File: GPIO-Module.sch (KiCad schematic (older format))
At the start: 41 parts

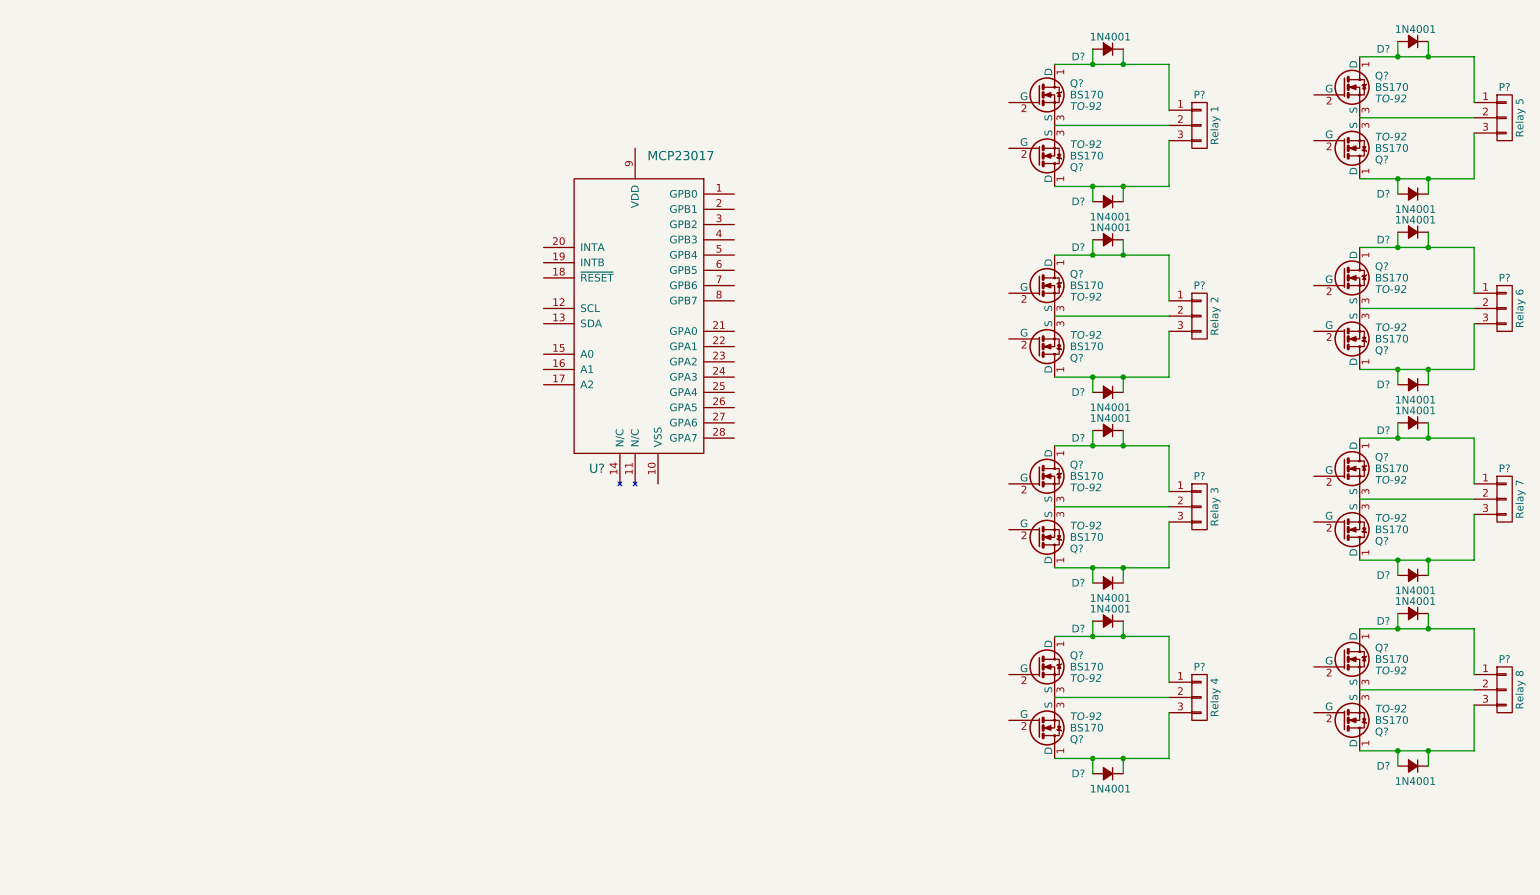
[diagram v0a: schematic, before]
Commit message: finished schematic and started pcb layout
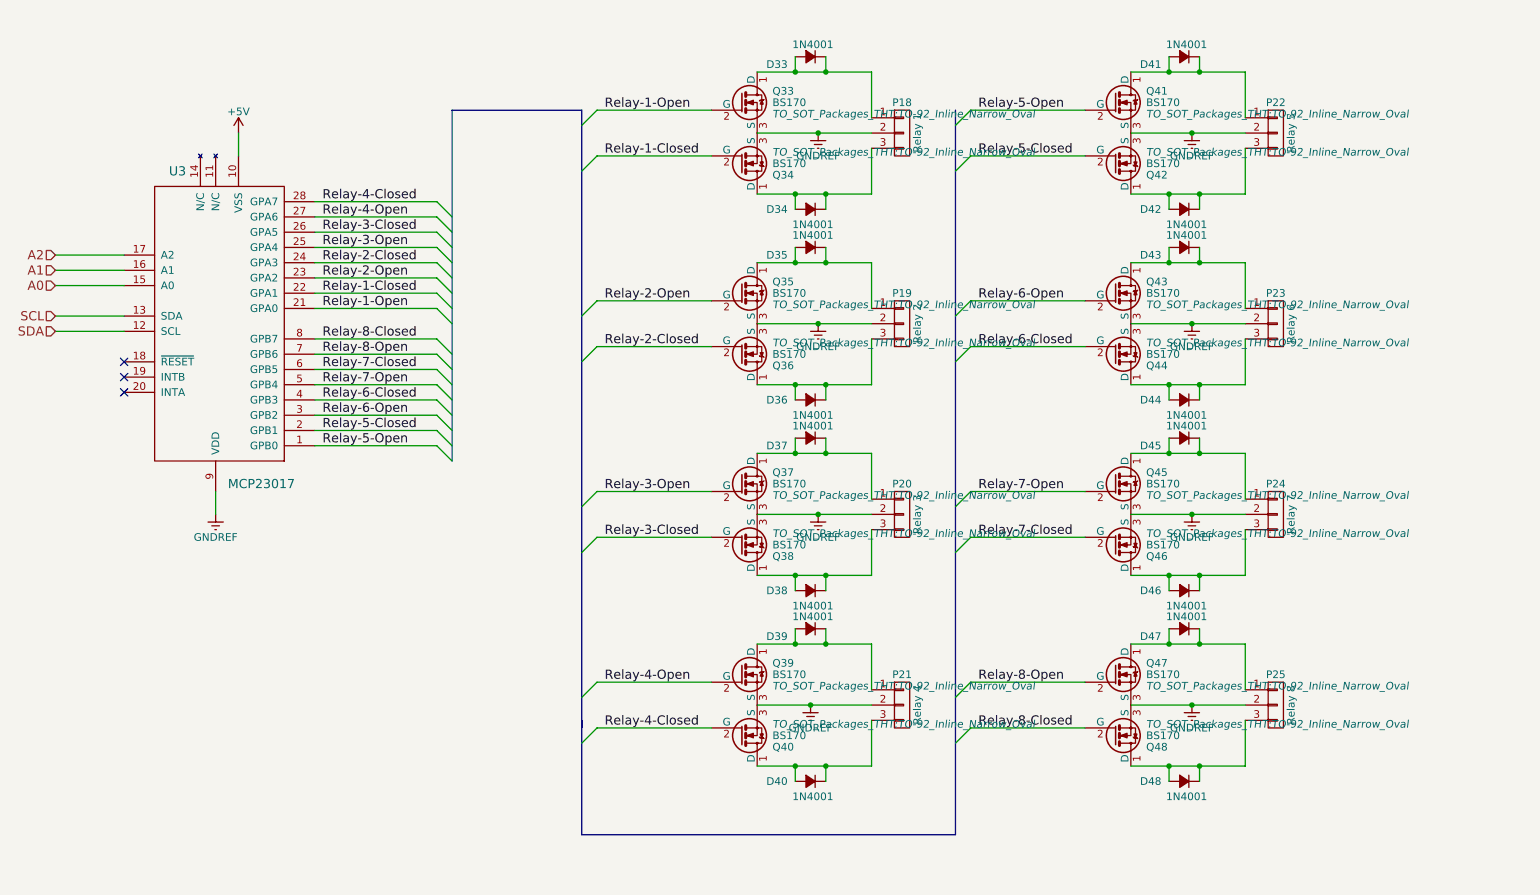
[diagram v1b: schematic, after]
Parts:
- D1, D10, D11, D12, D13, D14, D15, D16, D2, D3, D4, D5, D6, D7, D8, D9: renamed from D?; footprint (none) -> Diodes_ThroughHole:Diode_DO-41_SOD81_Horizontal_RM10
- P2, P3, P4, P5, P6, P7, P8, P9: renamed from P?; footprint (none) -> Terminal_Blocks:TerminalBlock_Pheonix_MPT-2.54mm_3pol
- Q1, Q10, Q11, Q12, Q13, Q14, Q15, Q16, Q2, Q3, Q4, Q5, Q6, Q7, Q8, Q9: renamed from Q?; footprint TO-92 -> TO_SOT_Packages_THT:TO-92_Inline_Narrow_Oval
- U1: renamed from U?; footprint (none) -> Housings_DIP:DIP-28_W7.62mm_LongPads
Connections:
- net Relay-5-Open: now reaches U1.1 (GPB0)
- net Relay-5-Open: now also Q9.2 (G)
- net +5V: now reaches U1.10 (VSS)
- net SDA: now reaches U1.12 (SCL)
- net SCL: now reaches U1.13 (SDA)
- net A0: now reaches U1.15 (A0)
- net A1: now reaches U1.16 (A1)
- net A2: now reaches U1.17 (A2)
- net Relay-5-Closed: now reaches U1.2 (GPB1)
- net Relay-5-Closed: now also Q10.2 (G)
- net Relay-1-Open: now reaches U1.21 (GPA0)
- net Relay-1-Open: now also Q1.2 (G)
- net Relay-1-Closed: now reaches U1.22 (GPA1)
- net Relay-1-Closed: now also Q2.2 (G)
- net Relay-2-Open: now reaches U1.23 (GPA2)
- net Relay-2-Open: now also Q3.2 (G)
- net Relay-2-Closed: now reaches U1.24 (GPA3)
- net Relay-2-Closed: now also Q4.2 (G)
- net Relay-3-Open: now reaches U1.25 (GPA4)
- net Relay-3-Open: now also Q5.2 (G)
- net Relay-3-Closed: now reaches U1.26 (GPA5)
- net Relay-3-Closed: now also Q6.2 (G)
- net Relay-4-Open: now reaches U1.27 (GPA6)
- net Relay-4-Open: now also Q7.2 (G)
- net Relay-4-Closed: now reaches U1.28 (GPA7)
- net Relay-4-Closed: now also Q8.2 (G)
- net Relay-6-Open: now reaches U1.3 (GPB2)
- net Relay-6-Open: now also Q11.2 (G)
- net Relay-6-Closed: now reaches U1.4 (GPB3)
- net Relay-6-Closed: now also Q12.2 (G)
- net Relay-7-Open: now reaches U1.5 (GPB4)
- net Relay-7-Open: now also Q13.2 (G)
- net Relay-7-Closed: now reaches U1.6 (GPB5)
- net Relay-7-Closed: now also Q14.2 (G)
- net Relay-8-Open: now reaches U1.7 (GPB6)
- net Relay-8-Open: now also Q15.2 (G)
- net Relay-8-Closed: now reaches U1.8 (GPB7)
- net Relay-8-Closed: now also Q16.2 (G)
- net GNDREF: now reaches U1.9 (VDD)
- net GNDREF: now also P2.2 (P2), P3.2 (P2), P4.2 (P2), P5.2 (P2), P6.2 (P2), P7.2 (P2), P8.2 (P2), P9.2 (P2), Q1.3 (S), Q10.3 (S), Q11.3 (S), Q12.3 (S), Q13.3 (S), Q14.3 (S), Q15.3 (S), Q16.3 (S), Q2.3 (S), Q3.3 (S), Q4.3 (S), Q5.3 (S), Q6.3 (S), Q7.3 (S), Q8.3 (S), Q9.3 (S)
- no-connect marks 0 -> 3
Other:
- moved on the sheet: D33, D34, D35, D36, D37, D38, D39, D40, D41, D42, D43, D44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

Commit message: fixed some schematic issues
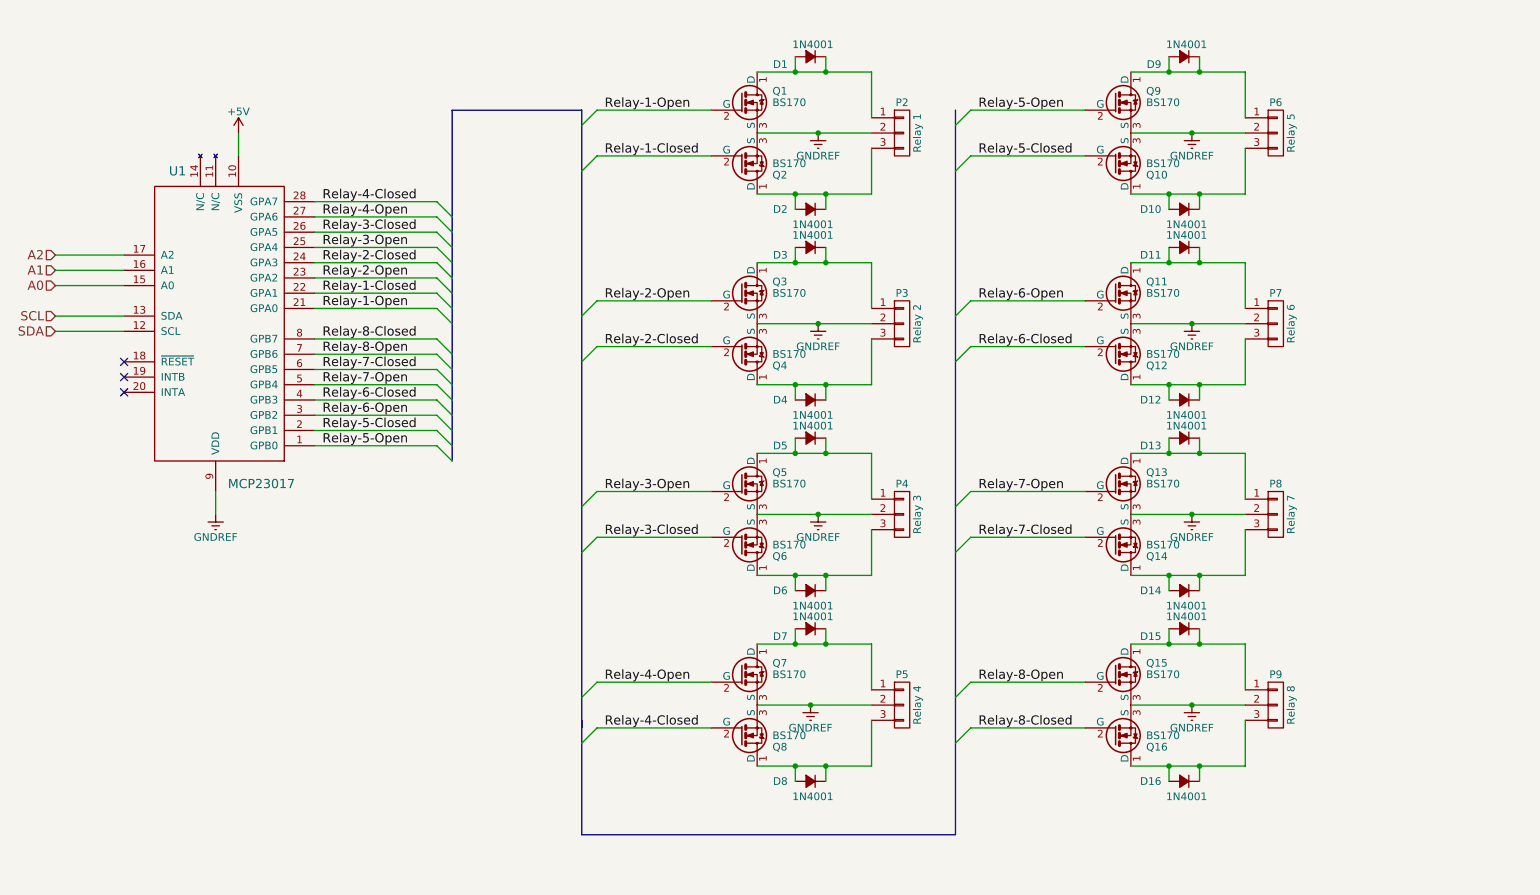
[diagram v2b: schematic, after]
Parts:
- Q1, Q10, Q11, Q12, Q13, Q14, Q15, Q16, Q2, Q3, Q5, Q6, Q7, Q8, Q9: Pricing (none) -> 0.00@0

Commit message: added relays to control AC voltages
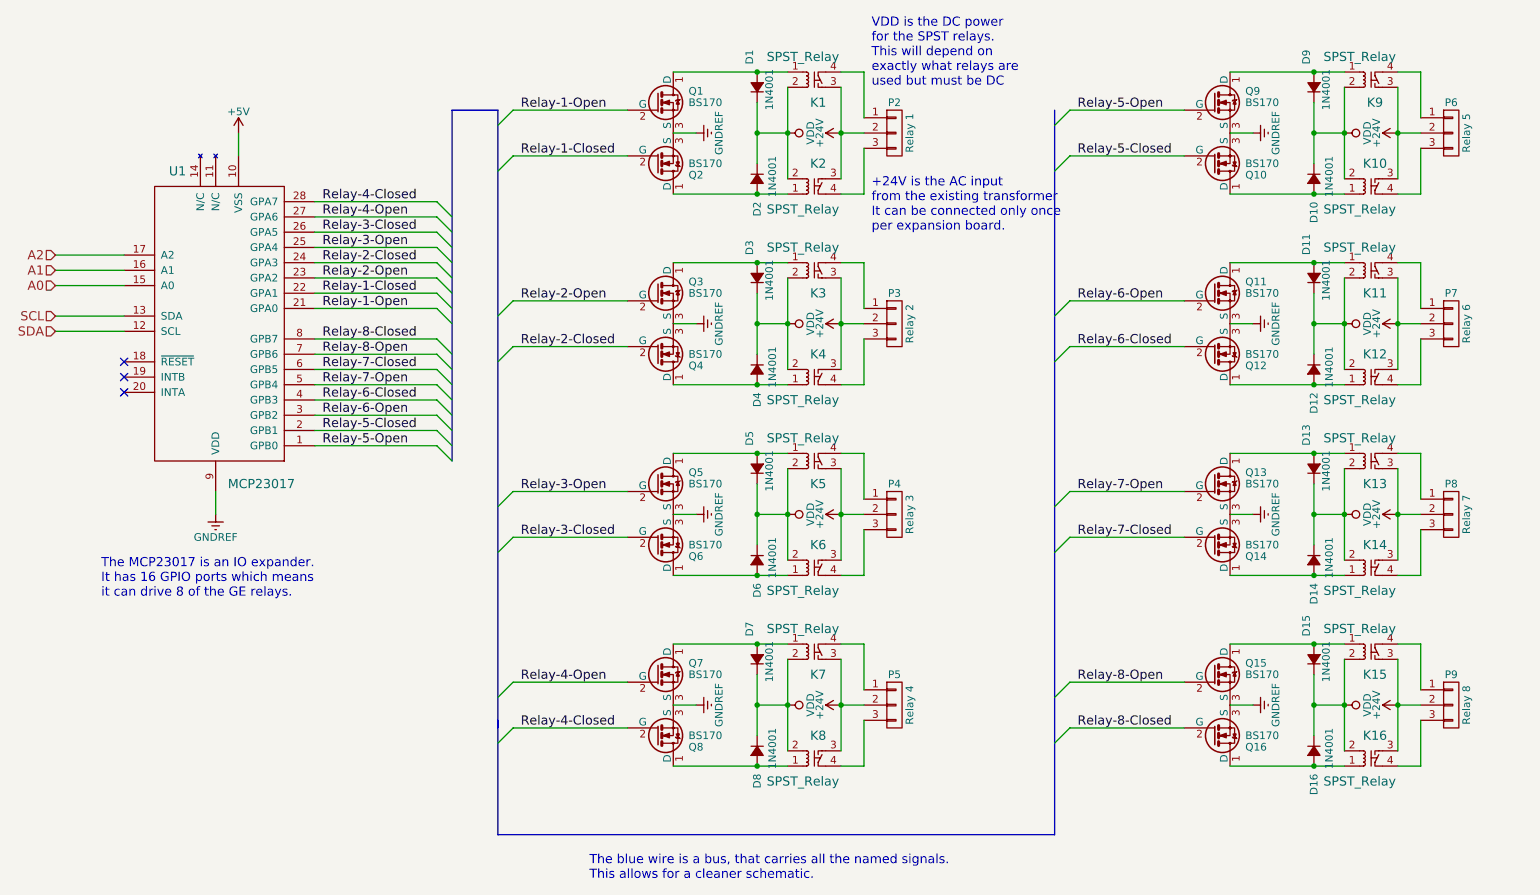
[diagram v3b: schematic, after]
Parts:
- added K1, K10, K11, K12, K13, K14, K15, K16, K2, K3, K4, K5, K6, K7, K8, K9: SPST_Relay, symbol SPST_Relay
- Q4: Pricing (none) -> 0.00@0
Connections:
- net GNDREF: no longer P2.2 (P2), P3.2 (P2), P4.2 (P2), P5.2 (P2), P6.2 (P2), P7.2 (P2), P8.2 (P2), P9.2 (P2)
- net at D9.2 (A), Q9.1 (D): now also K9.1 (Coil_1); no longer D9.1 (K), P6.1 (P1)
- net at D10.2 (A), Q10.1 (D): now also K10.1 (Coil_1); no longer D10.1 (K), P6.3 (P3)
- net at D11.2 (A), Q11.1 (D): now also K11.1 (Coil_1); no longer D11.1 (K), P7.1 (P1)
- net at D12.2 (A), Q12.1 (D): now also K12.1 (Coil_1); no longer D12.1 (K), P7.3 (P3)
- net at D13.2 (A), Q13.1 (D): now also K13.1 (Coil_1); no longer D13.1 (K), P8.1 (P1)
- net at D14.2 (A), Q14.1 (D): now also K14.1 (Coil_1); no longer D14.1 (K), P8.3 (P3)
- net at D15.2 (A), Q15.1 (D): now also K15.1 (Coil_1); no longer D15.1 (K), P9.1 (P1)
- net at D16.2 (A), Q16.1 (D): now also K16.1 (Coil_1); no longer D16.1 (K), P9.3 (P3)
- net at D1.2 (A), Q1.1 (D): now also K1.1 (Coil_1); no longer D1.1 (K), P2.1 (P1)
- net at D2.2 (A), Q2.1 (D): now also K2.1 (Coil_1); no longer D2.1 (K), P2.3 (P3)
- net at D3.2 (A), Q3.1 (D): now also K3.1 (Coil_1); no longer D3.1 (K), P3.1 (P1)
- net at D4.2 (A), Q4.1 (D): now also K4.1 (Coil_1); no longer D4.1 (K), P3.3 (P3)
- net at D5.2 (A), Q5.1 (D): now also K5.1 (Coil_1); no longer D5.1 (K), P4.1 (P1)
- net at D6.2 (A), Q6.1 (D): now also K6.1 (Coil_1); no longer D6.1 (K), P4.3 (P3)
- net at D7.2 (A), Q7.1 (D): now also K7.1 (Coil_1); no longer D7.1 (K), P5.1 (P1)
- net at D8.2 (A), Q8.1 (D): now also K8.1 (Coil_1); no longer D8.1 (K), P5.3 (P3)
- new net: K1.4 (Contact_B), P2.1 (P1)
- new net: K2.4 (Contact_B), P2.3 (P3)
- new net: K3.4 (Contact_B), P3.1 (P1)
- new net: K4.4 (Contact_B), P3.3 (P3)
- new net: K5.4 (Contact_B), P4.1 (P1)
- new net: K6.4 (Contact_B), P4.3 (P3)
- new net: K7.4 (Contact_B), P5.1 (P1)
- new net: K8.4 (Contact_B), P5.3 (P3)
- new net: K9.4 (Contact_B), P6.1 (P1)
- new net: K10.4 (Contact_B), P6.3 (P3)
- new net: K11.4 (Contact_B), P7.1 (P1)
- new net: K12.4 (Contact_B), P7.3 (P3)
- new net: K13.4 (Contact_B), P8.1 (P1)
- new net: K14.4 (Contact_B), P8.3 (P3)
- new net: K15.4 (Contact_B), P9.1 (P1)
- new net: K16.4 (Contact_B), P9.3 (P3)
- new net +24V: K1.3 (Contact_A), K10.3 (Contact_A), K11.3 (Contact_A), K12.3 (Contact_A), K13.3 (Contact_A), K14.3 (Contact_A), K15.3 (Contact_A), K16.3 (Contact_A), K2.3 (Contact_A), K3.3 (Contact_A), K4.3 (Contact_A), K5.3 (Contact_A), K6.3 (Contact_A), K7.3 (Contact_A), K8.3 (Contact_A), K9.3 (Contact_A), P2.2 (P2), P3.2 (P2), P4.2 (P2), P5.2 (P2), P6.2 (P2), P7.2 (P2), P8.2 (P2), P9.2 (P2)
- new net VDD: D1.1 (K), D10.1 (K), D11.1 (K), D12.1 (K), D13.1 (K), D14.1 (K), D15.1 (K), D16.1 (K), D2.1 (K), D3.1 (K), D4.1 (K), D5.1 (K), D6.1 (K), D7.1 (K), D8.1 (K), D9.1 (K), K1.2 (Coil_2), K10.2 (Coil_2), K11.2 (Coil_2), K12.2 (Coil_2), K13.2 (Coil_2), K14.2 (Coil_2), K15.2 (Coil_2), K16.2 (Coil_2), K2.2 (Coil_2), K3.2 (Coil_2), K4.2 (Coil_2), K5.2 (Coil_2), K6.2 (Coil_2), K7.2 (Coil_2), K8.2 (Coil_2), K9.2 (Coil_2)
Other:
- note added: "+24V is the AC input\nfrom the existing transformer\nIt can be connected only once\nper expansion board."
- note added: "The MCP23017 is an IO expander.\nIt has 16 GPIO ports which means\nit can drive 8 of the GE relays."
- note added: "The blue wire is a bus, that carries all the named signals.\nThis allows for a cleaner schematic."
- note added: "VDD is the DC power\nfor the SPST relays.\nThis will depend on\nexactly what relays are\nused but must be DC"
- moved on the sheet: D1, D2, P2, Q1, Q2
